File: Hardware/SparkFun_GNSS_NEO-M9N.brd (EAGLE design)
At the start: 64.9 x 38 mm, 55 parts, among them J1 MICROMOD_STANDARD, U1 U-BLOX_NEO-M9N, U2 3.3V, U3 EEPROM

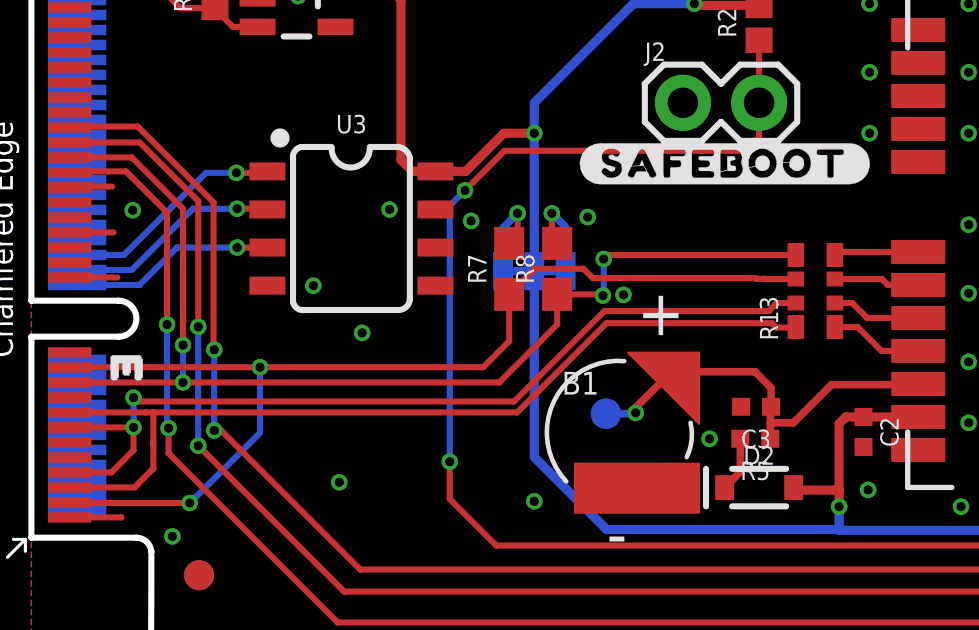
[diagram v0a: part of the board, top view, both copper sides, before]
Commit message: Correctly routes I2C to EEPROM chip
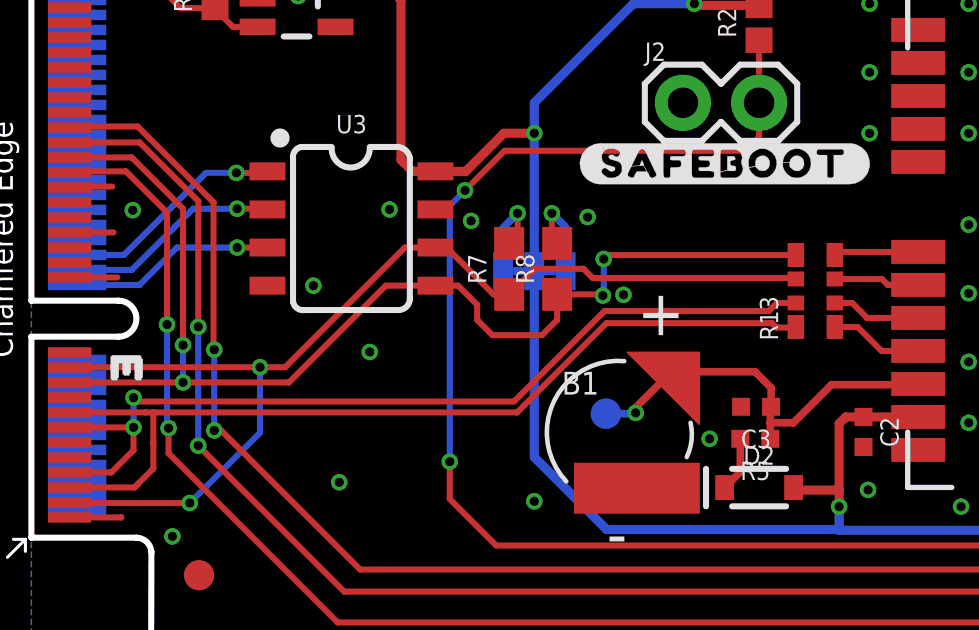
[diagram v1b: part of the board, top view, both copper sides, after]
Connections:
- removed net I2C_SCL: U3.6
- removed net I2C_SDA: U3.5
- net SCL/SCK: now also U3.6
- net SDA/!CS: now also U3.5
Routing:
- net SDA/!CS: track 37.6 -> 39.1 mm
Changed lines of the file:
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@@
 <setting verticaltext="up"/>
 </settings>
-<grid distance="0.01" unitdist="inch" unit="inch" style="dots" multiple="1" display="yes" altdistance="0.001" altunitdist="inch" altunit="inch"/>
+<grid distance="0.05" unitdist="inch" unit="inch" style="dots" multiple="1" display="yes" altdistance="0.005" altunitdist="inch" altunit="inch"/>
 <layers>
 <layer number="1" name="Top" color="4" fill="1" visible="yes" active="yes"/>
@@
 <via x="16.764" y="10.3378" extent="1-16" drill="0.3048"/>
 <via x="10.2616" y="10.9728" extent="1-16" drill="0.3048"/>
-<via x="11.0236" y="15.9512" extent="1-16" drill="0.3048"/>
+<via x="11.2776" y="15.3162" extent="1-16" drill="0.3048"/>
 <via x="3.3782" y="20.0406" extent="1-16" drill="0.3048"/>
 <via x="4.7752" y="29.3116" extent="1-16" drill="0.3048"/>
@@
 <wire x1="15.9258" y1="17.2348" x2="16.780603125" y2="18.0896" width="0.2032" layer="1"/>
 <wire x1="16.780603125" y1="18.0896" x2="18.4000875" y2="18.0896" width="0.2032" layer="1"/>
-<wire x1="24.13" y1="17.78" x2="24.1554" y2="17.7546" width="0.2032" layer="1"/>
-<wire x1="25.482" y1="17.7482" x2="24.466" y2="17.7482" width="0.2032" layer="1"/>
-<wire x1="24.466" y1="17.7482" x2="24.4596" y2="17.7546" width="0.2032" layer="1"/>
-<wire x1="24.4596" y1="17.7546" x2="24.1554" y2="17.7546" width="0.2032" layer="1"/>
-<wire x1="18.7096875" y1="17.78" x2="24.13" y2="17.78" width="0.2032" layer="1"/>
 <contactref element="J1" pad="3"/>
 <contactref element="J1" pad="21"/>
-<wire x1="15.9258" y1="15.6718" x2="15.9258" y2="17.2348" width="0.2032" layer="1"/>
 <via x="5.278046875" y="10.281846875" extent="1-16" drill="0.3048"/>
 <wire x1="5.278046875" y1="10.281846875" x2="7.62" y2="12.6238" width="0.2032" layer="16"/>
@@
 <wire x1="1.275" y1="14.8" x2="1.283" y2="14.808" width="0.2032" layer="1"/>
 <wire x1="7.62" y1="14.808" x2="1.283" y2="14.808" width="0.2032" layer="1"/>
-<wire x1="7.62" y1="14.808" x2="15.062" y2="14.808" width="0.2032" layer="1"/>
-<wire x1="15.062" y1="14.808" x2="15.9258" y2="15.6718" width="0.2032" layer="1"/>
 <wire x1="5.278046875" y1="10.281846875" x2="1.293153125" y2="10.281846875" width="0.2032" layer="1"/>
 <wire x1="1.293153125" y1="10.281846875" x2="1.275" y2="10.3" width="0.2032" layer="1"/>
+<contactref element="U3" pad="6"/>
+<wire x1="13.468" y1="18.796" x2="12.446" y2="18.796" width="0.2032" layer="1"/>
+<wire x1="8.458" y1="14.808" x2="7.62" y2="14.808" width="0.2032" layer="1"/>
+<wire x1="12.446" y1="18.796" x2="8.458" y2="14.808" width="0.2032" layer="1"/>
+<wire x1="13.468" y1="18.796" x2="13.843" y2="18.796" width="0.2032" layer="1"/>
+<wire x1="15.9258" y1="17.2348" x2="15.4042" y2="17.2348" width="0.2032" layer="1"/>
+<wire x1="15.4042" y1="17.2348" x2="13.843" y2="18.796" width="0.2032" layer="1"/>
+<wire x1="25.4502" y1="17.78" x2="25.482" y2="17.7482" width="0.2032" layer="1"/>
+<wire x1="18.7096875" y1="17.78" x2="25.4502" y2="17.78" width="0.2032" layer="1"/>
 </signal>
 <signal name="SDA/!CS">
@@
 <contactref element="J1" pad="49"/>
 <wire x1="1.275" y1="14.3" x2="5.0546" y2="14.3" width="0.2032" layer="1"/>
-<wire x1="5.0546" y1="14.3" x2="15.5954" y2="14.3" width="0.2032" layer="1"/>
-<wire x1="17.526" y1="16.2306" x2="17.526" y2="17.2348" width="0.2032" layer="1"/>
-<wire x1="15.5954" y1="14.3" x2="17.526" y2="16.2306" width="0.2032" layer="1"/>
 <wire x1="1.275" y1="21.8" x2="3.346" y2="21.8" width="0.2032" layer="1"/>
 <wire x1="5.0546" y1="20.0914" x2="5.0546" y2="15.5448" width="0.2032" layer="1"/>
@@
 <wire x1="5.0546" y1="15.5448" x2="5.0546" y2="14.3" width="0.2032" layer="16"/>
 <via x="5.0546" y="14.3" extent="1-16" drill="0.3048"/>
+<contactref element="U3" pad="5"/>
+<wire x1="5.0546" y1="14.3" x2="8.585" y2="14.3" width="0.2032" layer="1"/>
+<wire x1="11.811" y1="17.526" x2="13.468" y2="17.526" width="0.2032" layer="1"/>
+<wire x1="8.585" y1="14.3" x2="11.811" y2="17.526" width="0.2032" layer="1"/>
+<wire x1="13.468" y1="17.526" x2="14.224" y2="17.526" width="0.2032" layer="1"/>
+<wire x1="14.859" y1="16.891" x2="14.859" y2="16.383" width="0.2032" layer="1"/>
+<wire x1="14.859" y1="16.383" x2="15.367" y2="15.875" width="0.2032" layer="1"/>
+<wire x1="17.526" y1="16.383" x2="17.526" y2="17.2348" width="0.2032" layer="1"/>
+<wire x1="14.224" y1="17.526" x2="14.859" y2="16.891" width="0.2032" layer="1"/>
+<wire x1="15.367" y1="15.875" x2="17.018" y2="15.875" width="0.2032" layer="1"/>
+<wire x1="17.018" y1="15.875" x2="17.526" y2="16.383" width="0.2032" layer="1"/>
 </signal>
 <signal name="!RESET">
@@
 <wire x1="7.8426" y1="20.0914" x2="6.858" y2="20.0914" width="0.2032" layer="1"/>
 </signal>
-<signal name="I2C_SCL">
-<contactref element="U3" pad="6"/>
-</signal>
-<signal name="I2C_SDA">
-<contactref element="U3" pad="5"/>
-</signal>
 </signals>

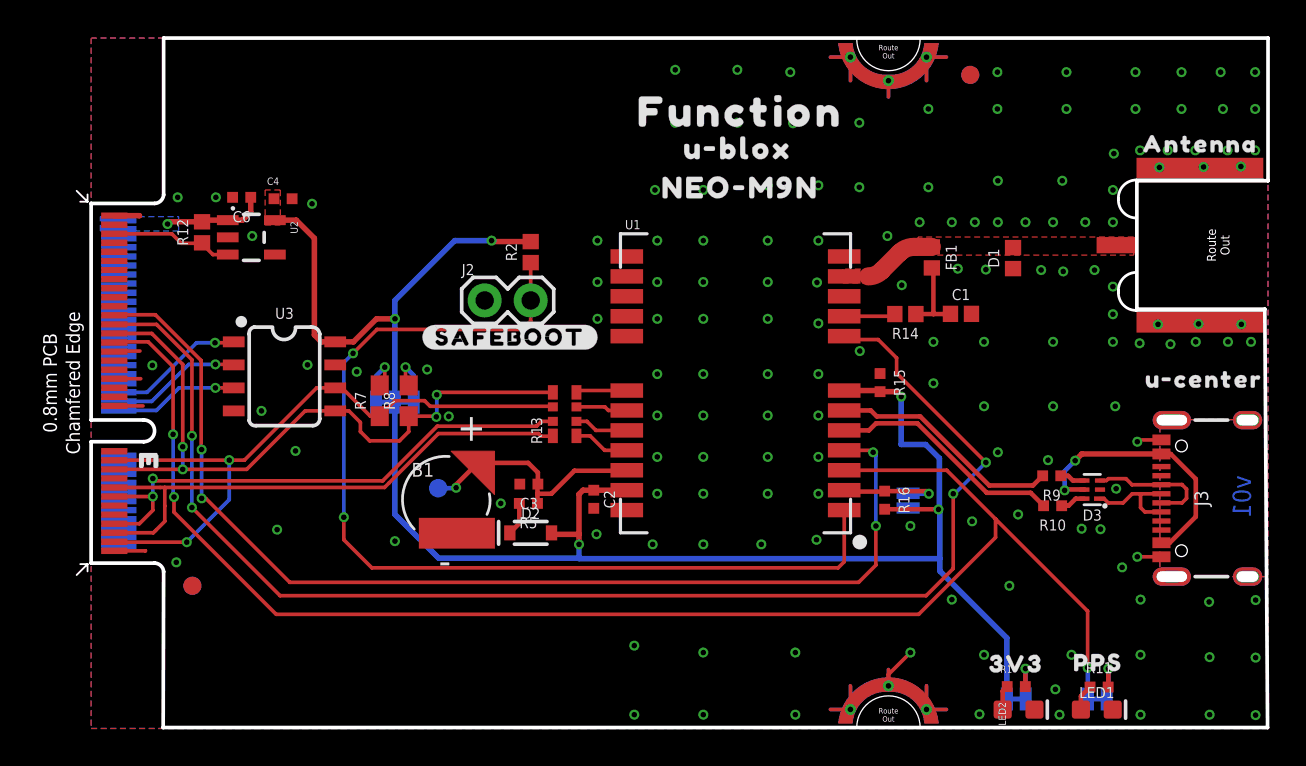
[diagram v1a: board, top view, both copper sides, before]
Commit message: Moves to 0603 components where they can be, updates measures
* Moves around vias for symmetrical appeal (though I burned out and so it's not)
* Adds silk
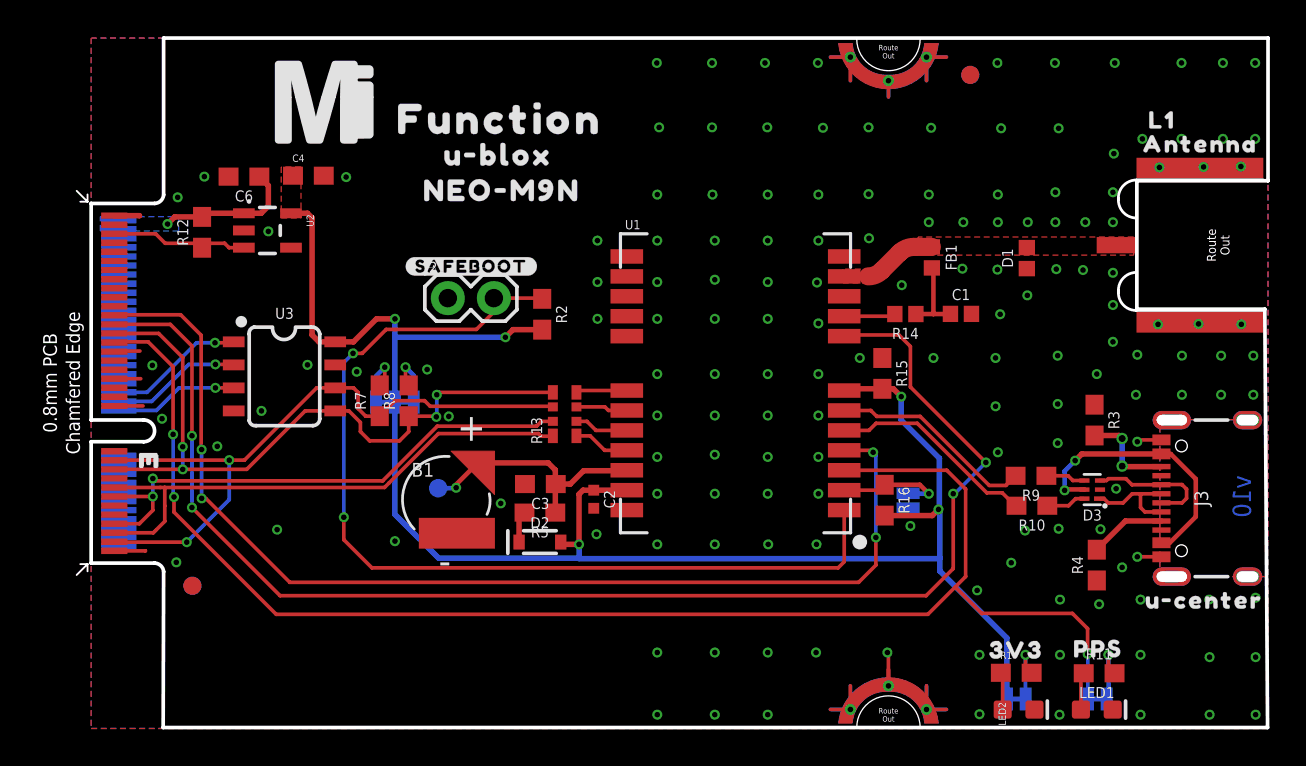
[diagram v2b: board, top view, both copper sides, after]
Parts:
- added R3, R4: 5.1k, SparkFun-Resistors:0603
- added U$11: (no value), SparkFun-MicroMod:MICROMOD_MI_LOGO_1
- added U$12: (no value), top:#3V3_LED#17
- added U$13: (no value), top:#PPS_LED#17
- added U$14: (no value), top:L1321542
- C3, C4, C6: device SparkFun-Capacitors:0402-TIGHT -> SparkFun-Capacitors:0603
- R1, R11, R15, R16, R5: device SparkFun-Resistors:0402-TIGHT -> SparkFun-Resistors:0603
- R10, R9: value 27OHM -> 27; device SparkFun-Resistors:0402-TIGHT -> SparkFun-Resistors:0603
- R12: value 100K -> 100k; device SparkFun-Resistors:0402 -> SparkFun-Resistors:0603
- R2: device SparkFun-Resistors:0402 -> SparkFun-Resistors:0603
- U$4: device top:#SAFEBOOT#16 -> top:#SAFEBOOT#12
- moved LOGO2 21.0 mm to (35.7, 21.1)
- moved FRAME1 20.1 mm to (1.27, -24.1)
- moved U$3 13.3 mm to (22.5, 33.6)
- moved U$5 13.2 mm to (22.5, 31.6)
- moved U$6 13.2 mm to (22.7, 29.7)
- moved U$9 12.2 mm to (61.4, 7.08)
- moved U$4 4.46 mm to (21.0, 25.5)
- moved R2 3.49 mm to (24.9, 22.9), turned to 270 degrees
- moved J2 2.04 mm to (19.7, 23.7)
- moved C4 1.89 mm to (12.0, 30.5)
- moved C6 1.15 mm to (8.43, 30.5)
- moved R10 1.14 mm to (51.9, 12.3)
- moved R9 1.14 mm to (51.9, 13.9)
- moved U2 0.97 mm to (9.73, 27.5)
- moved R5 0.81 mm to (24.8, 11.9)
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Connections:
- new net N$7: J3.A5, R4.2
- new net N$9: J3.B5, R3.2
- net GND: now also R3.1, R4.1
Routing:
- net N$9: track 0.00 -> 5.30 mm, vias 0 -> 2
- net N$7: track 0.00 -> 4.22 mm
- net 3.3V: track 99.0 -> 96.3 mm
- net VCC: track 5.68 -> 7.80 mm
- net !SAFE: track 55.5 -> 53.9 mm
- net N$12: track 13.0 -> 11.6 mm
- net N$11: track 12.9 -> 11.4 mm
- net !RESET: track 75.7 -> 77.1 mm
- net PPS: track 83.8 -> 82.9 mm
- net EN: track 6.79 -> 7.72 mm
- net N$1: track 2.68 -> 3.58 mm
- net N$4: track 2.74 -> 3.64 mm
- net INT: track 60.9 -> 61.7 mm
- net D+: track 1.41 -> 2.21 mm
- net D-: track 1.42 -> 2.21 mm
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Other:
- board text added: "v10"
- board text removed: "v01"

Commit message: Routes new switching ICs
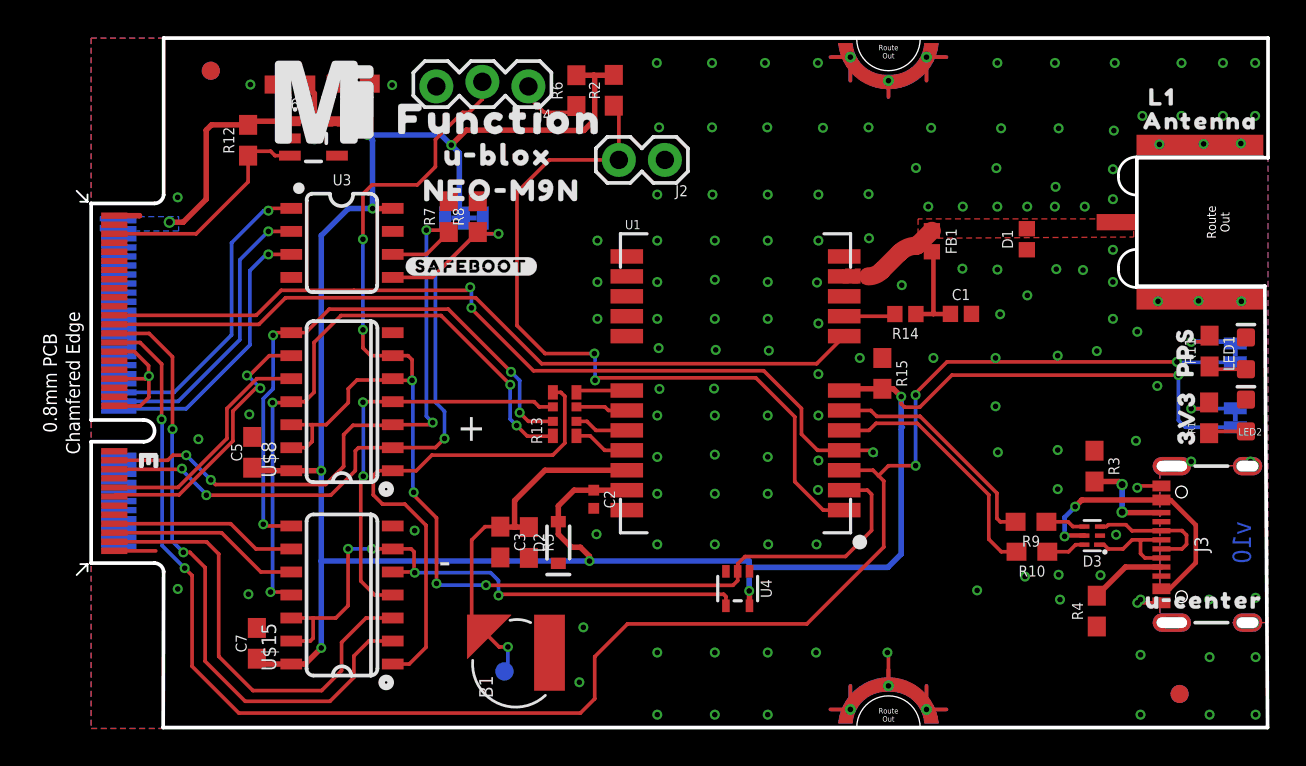
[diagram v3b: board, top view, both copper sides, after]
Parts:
- removed FRAME1: FRAME-LETTER, SparkFun-Aesthetics:CREATIVE_COMMONS
- removed R16: 1k, SparkFun-Resistors:0603
- removed SPI: JUMPER-SMT_2_NO_SILK, SparkFun-Jumpers:SMT-JUMPER_2_NO_SILK
- added C5, C7: 0.1uF, SparkFun-Capacitors:0603
- added FRAME2: FRAME-LEDGER, SparkFun-Aesthetics:CREATIVE_COMMONS
- added J4: (no value), SparkFun-Connectors:1X03_LOCK
- added R6: 10k, SparkFun-Resistors:0603
- added U$15: 74LVC4066D_QUAD_BILATERAL_SWITCH, SparkFun-IC-Logic:SO14
- added U4: 74HC1G04, SparkFun-IC-Logic:SOT353
- R7, R8: value 2.2k -> 4.7k
- U$8: value (none) -> 74LVC4066D_QUAD_BILATERAL_SWITCH; device top:#SPI#17 -> SparkFun-IC-Logic:SO14
- moved FD3 54.8 mm to (60.1, 1.90)
- moved FD4 54.8 mm to (60.1, 1.90)
- moved FD1 41.9 mm to (6.60, 36.3)
- moved FD2 41.9 mm to (6.60, 36.3)
- moved U$8 31.4 mm to (13.8, 17.4), flipped to the top, turned to 90 degrees
- moved LED1 21.3 mm to (63.7, 20.7), turned to 90 degrees
- moved PPS 20.6 mm to (63.1, 20.7), turned to 270 degrees
- moved LED2 20.5 mm to (63.7, 17.3), turned to 90 degrees
- moved PWR\ 19.7 mm to (63.1, 17.1), turned to 270 degrees
- moved R11 18.8 mm to (61.7, 20.8), turned to 90 degrees
- moved R1 17.6 mm to (61.7, 17.1), turned to 90 degrees
- moved U$2 17.1 mm to (60.4, 20.8), turned to 90 degrees
- moved U$13 16.1 mm to (59.6, 20.8), turned to 180 degrees
- moved U$1 15.9 mm to (60.5, 17.1), turned to 90 degrees
- moved U$12 14.6 mm to (59.5, 17.2), turned to 180 degrees
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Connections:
- removed net SDA/!CS: J1.19, J1.49, R13.P5, R8.1, U3.5
- new net INV_D_SEL: U$15.12, U$15.13, U$15.5, U$15.6, U4.4
- new net N$13: J4.1, R6.1
- new net RXI: J1.15, U$8.10
- new net SCK: J1.3, U$15.3
- new net SCL: J1.21, R7.1, U$8.3, U3.6
- new net SDA: J1.19, R8.1, U$8.2, U3.5
- new net SDA/SPI_!CS!: R13.P5, U$15.1, U$8.1
- new net SDI: J1.5, U$15.10
- new net SDO: J1.7, U$15.9
- new net SPI_!CS!: J1.49, U$15.2
- new net TXO: J1.13, U$8.9
- net 3.3V: now also C5.1, C7.1, R6.2, U$15.14, U$8.14, U4.5; no longer R16.2
- net D_SEL: now also J4.2, U$8.12, U$8.13, U$8.5, U$8.6, U4.2; no longer R16.1, SPI.2
- net GND: now also C5.2, C7.2, J4.3, U$15.7, U$8.7, U4.3; no longer SPI.1
- net RXI/SDI: now also U$15.11, U$8.11; no longer J1.15, J1.5
- net SCL/SCK: now also U$15.4, U$8.4; no longer J1.21, J1.3, R7.1, U3.6
- net TXO/SDO: now also U$15.8, U$8.8; no longer J1.13, J1.7
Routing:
- net D_SEL: track 6.53 -> 74.9 mm, vias 1 -> 6
- net 3.3V: track 96.3 -> 141.3 mm, vias 5 -> 9
- net SDA: track 0.00 -> 41.4 mm, vias 0 -> 4
- net SDA/!CS: track 39.4 -> 0.00 mm, vias 4 -> 0
- net SCL: track 0.00 -> 36.4 mm, vias 0 -> 4
- net SPI_!CS!: track 0.00 -> 34.9 mm, vias 0 -> 2
- net !RESET: track 77.1 -> 43.1 mm, vias 4 -> 0
- net INV_D_SEL: track 0.00 -> 33.8 mm, vias 0 -> 4
- net SDA/SPI_!CS!: track 0.00 -> 28.3 mm
- net SCK: track 0.00 -> 24.7 mm
- net TXO: track 0.00 -> 15.4 mm, vias 0 -> 2
- net SCL/SCK: track 37.0 -> 22.7 mm
- net INT: track 61.7 -> 48.0 mm, vias 4 -> 3
- net RXI: track 0.00 -> 13.2 mm
- net PPS: track 82.9 -> 95.6 mm, vias 3 -> 5
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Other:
- outline, holes or cut-outs redrawn
